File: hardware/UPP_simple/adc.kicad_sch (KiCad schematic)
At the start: 3 parts, among them IC1 ADS114S08BIPBSR

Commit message: Add files via upload
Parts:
- removed C1: 330n, Capacitor_SMD:C_0603_1608Metric_Pad1.08x0.95mm_HandSolder, symbol Device:C
- removed IC1: ADS114S08BIPBSR, QFP50P700X700X120-32N, symbol ADS114S08BIPBSR:ADS114S08BIPBSR
- added C2, C4: 100n, Capacitor_SMD:C_0603_1608Metric, symbol Device:C_Small
- added U2: ADS114S08BIPBSR, adc:QFP50P700X700X120-32N, symbol ADS114S08BIPBSR:ADS114S08BIPBSR
- C3: renamed from C2; value 330n -> 1u
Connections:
- net +5V: now also C2.1, U2.26 (AVDD)
- net ADC.DRDY: now also U2.13 (~{DRDY})
- net ADC.RST: now also U2.18 (~{RESET})
- net ADC.START: now also U2.8 (START/SYNC)
- net ADC_SPI.CLK: now also U2.11 (SCLK)
- net ADC_SPI.MISO: now also U2.12 (DOUT/~{DRDY})
- net ADC_SPI.MOSI: now also U2.10 (DIN)
- net DIF1: now also U2.32 (REFP1/AIN6)
- net DIF2: now also U2.31 (REFN1/AIN7)
- net DIF3: now also U2.22 (GPIO0/AIN8)
- net DIF4: now also U2.21 (GPIO1/AIN9)
- net DIF5: now also U2.20 (GPIO2/AIN10)
- net DIF6: now also U2.19 (GPIO3/AIN11)
- net GND: now also C2.2, C4.2, U2.14 (DGND), U2.17 (CLK), U2.24 (REFCOM), U2.27 (AVSS_1), U2.28 (AVSS_2)
- net SE1: now also U2.7 (AIN0)
- net SE2: now also U2.6 (AIN1)
- net SE3: now also U2.5 (AIN2)
- net SE4: now also U2.4 (AIN3)
- net SE5: now also U2.3 (AIN4)
- net SE6: now also U2.2 (AIN5)
- net at C3.1: now also U2.23 (REFOUT)
- new net 3V3: C4.1, U2.15 (IOVDD), U2.16 (DVDD)
- new net ADC_SPI.NSS: U2.9 (~{CS})
- no-connect marks 5 -> 3
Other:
- moved on the sheet: C3

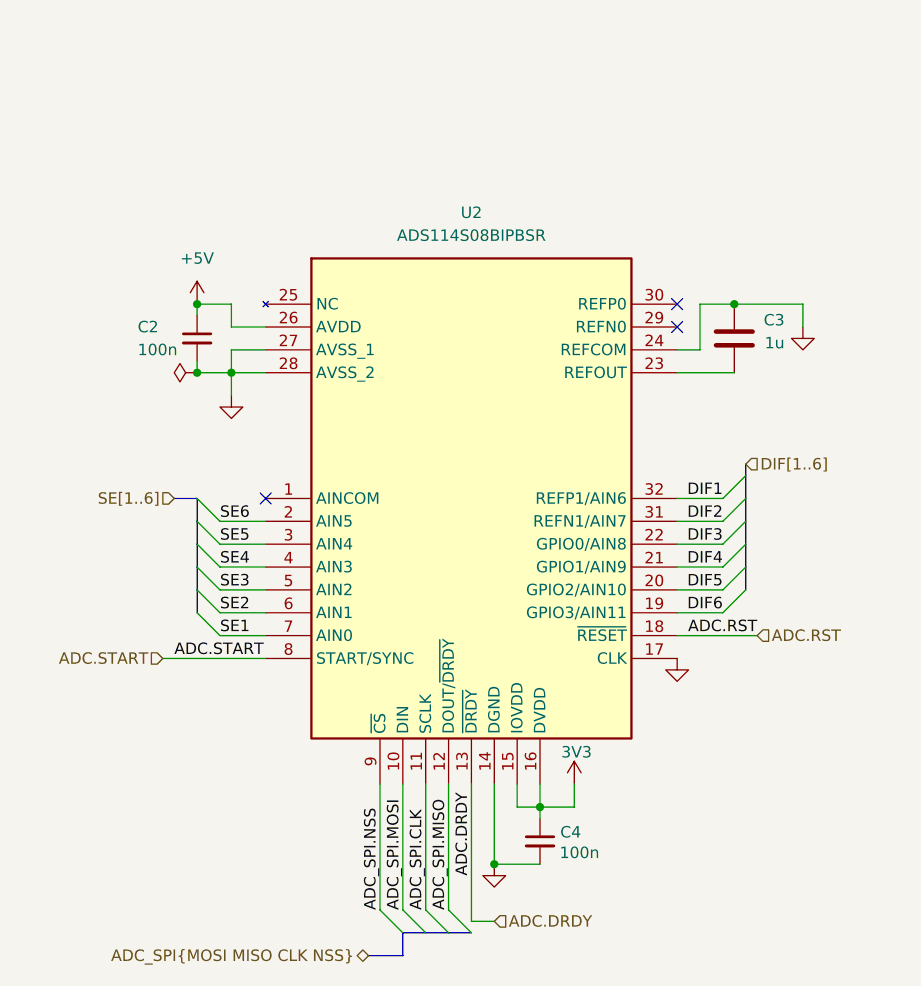
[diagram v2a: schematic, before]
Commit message: Changed Opamps cleared schematic
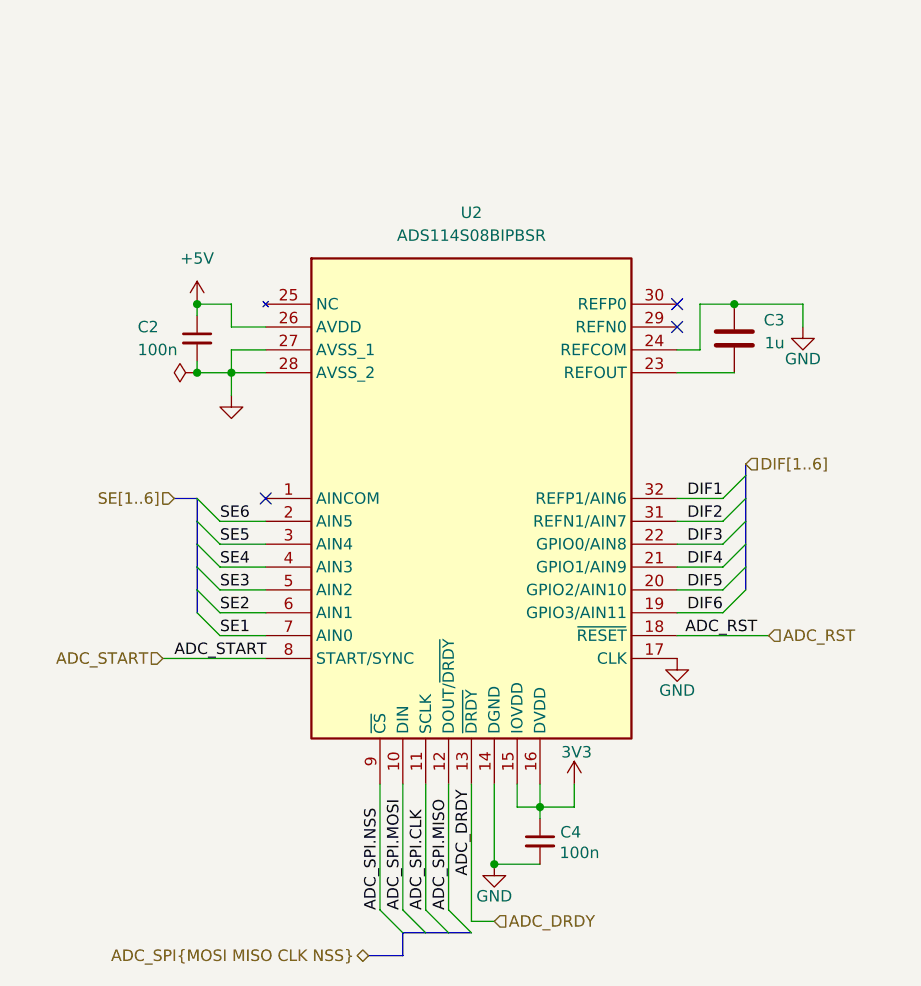
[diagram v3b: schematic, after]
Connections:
- net ADC.DRDY renamed ADC_DRDY
- net ADC.RST renamed ADC_RST
- net ADC.START renamed ADC_START
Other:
- title: Universal use measuring PCB -> Universal Measurement Board
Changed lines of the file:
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@@
 	(paper "A4")
 	(title_block
-		(title "Universal use measuring PCB")
+		(title "Universal Measurement Board")
 		(rev "1")
 		(company "Author: Kacper Pawlak")
@@
 	(wire
 		(pts
-			(xy 171.45 107.95) (xy 180.34 107.95)
+			(xy 171.45 107.95) (xy 181.61 107.95)
 		)
 		(stroke
@@
 		)
 	)
-	(label "ADC.RST"
+	(label "ADC_RST"
 		(at 180.34 107.95 180)
 		(effects
@@
 		)
 	)
-	(label "ADC.DRDY"
+	(label "ADC_DRDY"
 		(at 148.59 134.62 90)
 		(effects
@@
 		)
 	)
-	(label "ADC.START"
+	(label "ADC_START"
 		(at 115.57 110.49 0)
 		(effects
@@
 		)
 	)
-	(hierarchical_label "ADC.DRDY"
+	(hierarchical_label "ADC_DRDY"
 		(shape input)
 		(at 151.13 139.7 0)
@@
 		)
 	)
-	(hierarchical_label "ADC.RST"
+	(hierarchical_label "ADC_RST"
 		(shape input)
-		(at 180.34 107.95 0)
+		(at 181.61 107.95 0)
 		(effects
 			(font
@@
 		)
 	)
-	(hierarchical_label "ADC.START"
+	(hierarchical_label "ADC_START"
 		(shape input)
 		(at 114.3 110.49 180)
@@
 	(symbol
 		(lib_id "power:GND")
-		(at 171.45 110.49 0)
+		(at 185.42 73.66 0)
 		(unit 1)
 		(exclude_from_sim no)
@@
 		(on_board yes)
 		(dnp no)
-		(fields_autoplaced yes)
-		(property "Reference" "#PWR017"
-			(at 171.45 116.84 0)
+		(property "Reference" "#PWR016"
+			(at 185.42 80.01 0)
 			(effects
 				(font
@@
 		)
 		(property "Value" "GND"
-			(at 171.45 115.57 0)
-			(effects
-				(font
-					(size 1.27 1.27)
-				)
-				(hide yes)
+			(at 185.42 77.216 0)
+			(effects
+				(font
+					(size 1.27 1.27)
+				)
 			)
 		)
 		(property "Footprint" ""
-			(at 171.45 110.49 0)
+			(at 185.42 73.66 0)
 			(effects
 				(font
@@
 		)
 		(property "Datasheet" ""
-			(at 171.45 110.49 0)
+			(at 185.42 73.66 0)
 			(effects
 				(font
@@
 		)
 		(property "Description" "Power symbol creates a global label with name \"GND\" , ground"
-			(at 171.45 110.49 0)
+			(at 185.42 73.66 0)
 			(effects
 				(font
@@
 		)
 		(instances
-			(project "upp_simple"
+			(project "UMB"
 				(path "/b652b05a-4e3d-4ad1-b032-18886abe7d45/27728c5b-995e-4e9b-804c-adae9f98b692"
-					(reference "#PWR017")
+					(reference "#PWR016")
 					(unit 1)
 				)
@@
 	)
 	(symbol
-		(lib_id "power:GND")
-		(at 151.13 133.35 0)
-		(mirror y)
-		(unit 1)
-		(exclude_from_sim no)
-		(in_bom yes)
-		(on_board yes)
-		(dnp no)
-		(fields_autoplaced yes)
-		(property "Reference" "#PWR083"
-			(at 151.13 139.7 0)
-			(effects
-				(font
-					(size 1.27 1.27)
-				)
-				(hide yes)
-			)
-		)
-		(property "Value" "GND"
-			(at 151.13 138.43 0)
-			(effects
-				(font
-					(size 1.27 1.27)
-				)
-				(hide yes)
-			)
-		)
-		(property "Footprint" ""
-			(at 151.13 133.35 0)
-			(effects
-				(font
-					(size 1.27 1.27)
-				)
-				(hide yes)
-			)
-		)
-		(property "Datasheet" ""
-			(at 151.13 133.35 0)
-			(effects
-				(font
-					(size 1.27 1.27)
-				)
-				(hide yes)
-			)
-		)
-		(property "Description" "Power symbol creates a global label with name \"GND\" , ground"
-			(at 151.13 133.35 0)
-			(effects
-				(font
-					(size 1.27 1.27)
-				)
-				(hide yes)
-			)
-		)
-		(pin "1"
-		)
-		(instances
-			(project "upp_simple"
-				(path "/b652b05a-4e3d-4ad1-b032-18886abe7d45/27728c5b-995e-4e9b-804c-adae9f98b692"
-					(reference "#PWR083")
-					(unit 1)
-				)
-			)
-		)
-	)
-	(symbol
 		(lib_name "ADS114S08BIPBSR_1")
 		(lib_id "ADS114S08BIPBSR:ADS114S08BIPBSR")
@@
 	)
 	(symbol
-		(lib_id "power:GND")
-		(at 185.42 73.66 0)
-		(mirror y)
-		(unit 1)
-		(exclude_from_sim no)
-		(in_bom yes)
-		(on_board yes)
-		(dnp no)
-		(fields_autoplaced yes)
-		(property "Reference" "#PWR016"
-			(at 185.42 80.01 0)
-			(effects
-				(font
-					(size 1.27 1.27)
-				)
-				(hide yes)
-			)
-		)
-		(property "Value" "GND"
-			(at 185.42 78.74 0)
-			(effects
-				(font
-					(size 1.27 1.27)
-				)
-				(hide yes)
-			)
-		)
-		(property "Footprint" ""
-			(at 185.42 73.66 0)
-			(effects
-				(font
-					(size 1.27 1.27)
-				)
-				(hide yes)
-			)
-		)
-		(property "Datasheet" ""
-			(at 185.42 73.66 0)
-			(effects
-				(font
-					(size 1.27 1.27)
-				)
-				(hide yes)
-			)
-		)
-		(property "Description" "Power symbol creates a global label with name \"GND\" , ground"
-			(at 185.42 73.66 0)
-			(effects
-				(font
-					(size 1.27 1.27)
-				)
-				(hide yes)
-			)
-		)
-		(pin "1"
-		)
-		(instances
-			(project "UPP_simple"
-				(path "/b652b05a-4e3d-4ad1-b032-18886abe7d45/27728c5b-995e-4e9b-804c-adae9f98b692"
-					(reference "#PWR016")
-					(unit 1)
-				)
-			)
-		)
-	)
-	(symbol
 		(lib_id "power:PWR_FLAG")
 		(at 118.11 78.74 90)
@@
 	)
 	(symbol
+		(lib_id "power:GND")
+		(at 171.45 110.49 0)
+		(unit 1)
+		(exclude_from_sim no)
+		(in_bom yes)
+		(on_board yes)
+		(dnp no)
+		(property "Reference" "#PWR017"
+			(at 171.45 116.84 0)
+			(effects
+				(font
+					(size 1.27 1.27)
+				)
+				(hide yes)
+			)
+		)
+		(property "Value" "GND"
+			(at 171.45 114.046 0)
+			(effects
+				(font
+					(size 1.27 1.27)
+				)
+			)
+		)
+		(property "Footprint" ""
+			(at 171.45 110.49 0)
+			(effects
+				(font
+					(size 1.27 1.27)
+				)
+				(hide yes)
+			)
+		)
+		(property "Datasheet" ""
+			(at 171.45 110.49 0)
+			(effects
+				(font
+					(size 1.27 1.27)
+				)
+				(hide yes)
+			)
+		)
+		(property "Description" "Power symbol creates a global label with name \"GND\" , ground"
+			(at 171.45 110.49 0)
+			(effects
+				(font
+					(size 1.27 1.27)
+				)
+				(hide yes)
+			)
+		)
+		(pin "1"
+		)
+		(instances
+			(project "UMB"
+				(path "/b652b05a-4e3d-4ad1-b032-18886abe7d45/27728c5b-995e-4e9b-804c-adae9f98b692"
+					(reference "#PWR017")
+					(unit 1)
+				)
+			)
+		)
+	)
+	(symbol
 		(lib_id "Device:C")
 		(at 177.8 74.93 180)
@@
 					(unit 1)
 				)
+			)
+		)
+	)
+	(symbol
+		(lib_id "power:GND")
+		(at 151.13 133.35 0)
+		(unit 1)
+		(exclude_from_sim no)
+		(in_bom yes)
+		(on_board yes)
+		(dnp no)
+		(property "Reference" "#PWR044"
+			(at 151.13 139.7 0)
+			(effects
+				(font
+					(size 1.27 1.27)
+				)
+				(hide yes)
+			)
+		)
+		(property "Value" "GND"
+			(at 151.13 136.906 0)
+			(effects
+				(font
+					(size 1.27 1.27)
+				)
+			)
+		)
+		(property "Footprint" ""
+			(at 151.13 133.35 0)
+			(effects
+				(font
+					(size 1.27 1.27)
+				)
+				(hide yes)
+			)
+		)
+		(property "Datasheet" ""
+			(at 151.13 133.35 0)
+			(effects
+				(font
+					(size 1.27 1.27)
+				)
+				(hide yes)
+			)
+		)
+		(property "Description" "Power symbol creates a global label with name \"GND\" , ground"
+			(at 151.13 133.35 0)
+			(effects
+				(font
+					(size 1.27 1.27)
+				)
+				(hide yes)
+			)
+		)
+		(pin "1"
+		)
+		(instances
+			(project "UMB"
+				(path "/b652b05a-4e3d-4ad1-b032-18886abe7d45/27728c5b-995e-4e9b-804c-adae9f98b692"
+					(reference "#PWR044")
+					(unit 1)
+				)
